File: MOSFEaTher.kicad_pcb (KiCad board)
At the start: 2 copper layers, 63.5 x 51.5 mm, 33 parts, among them J1 GPIO 13, J2 GPIO 12, J3 GPIO 27, J4 GPIO 21, J5 GPIO 33, J6 GPIO 15, J7 GPIO 32, J8 GPIO 14, Q1 STD7NK40Z, Q2 STD7NK40Z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

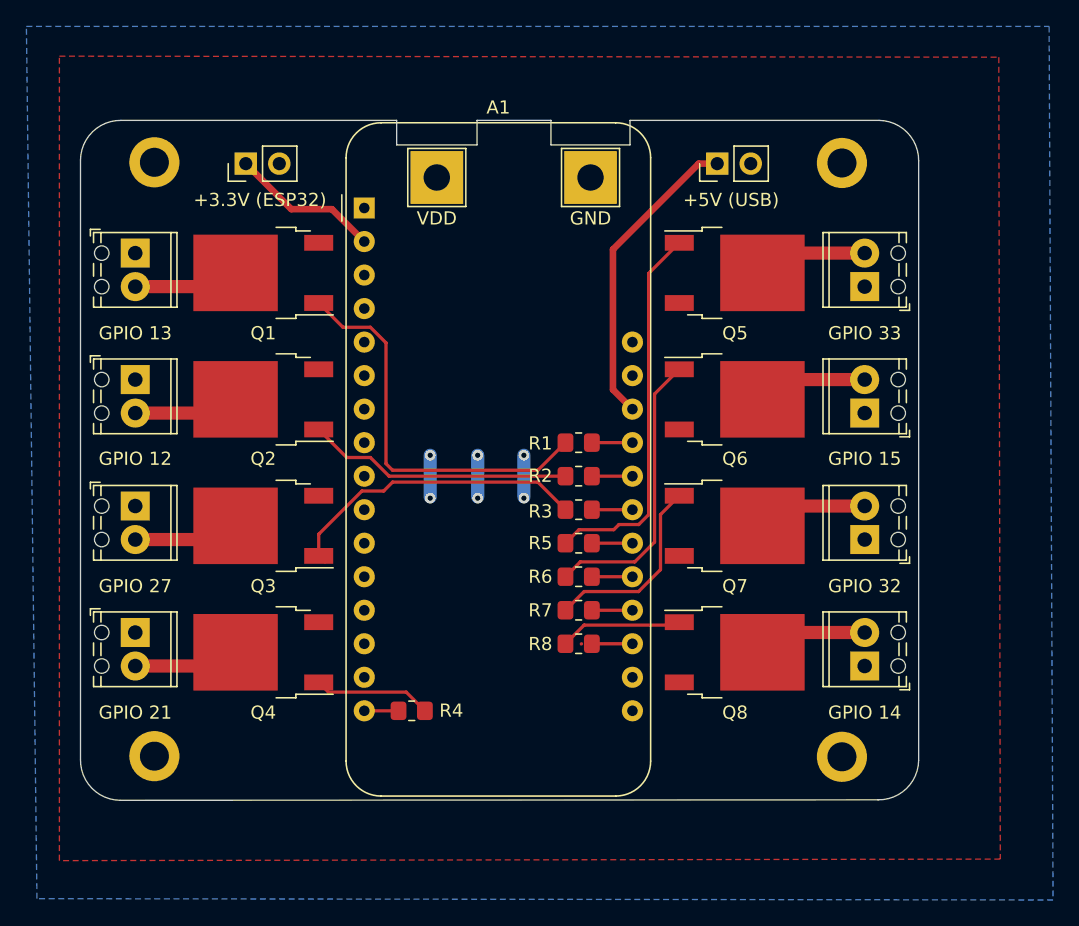
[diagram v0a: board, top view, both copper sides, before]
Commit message: feat: M3 mounting holes, OSHW logo and THM affiliation
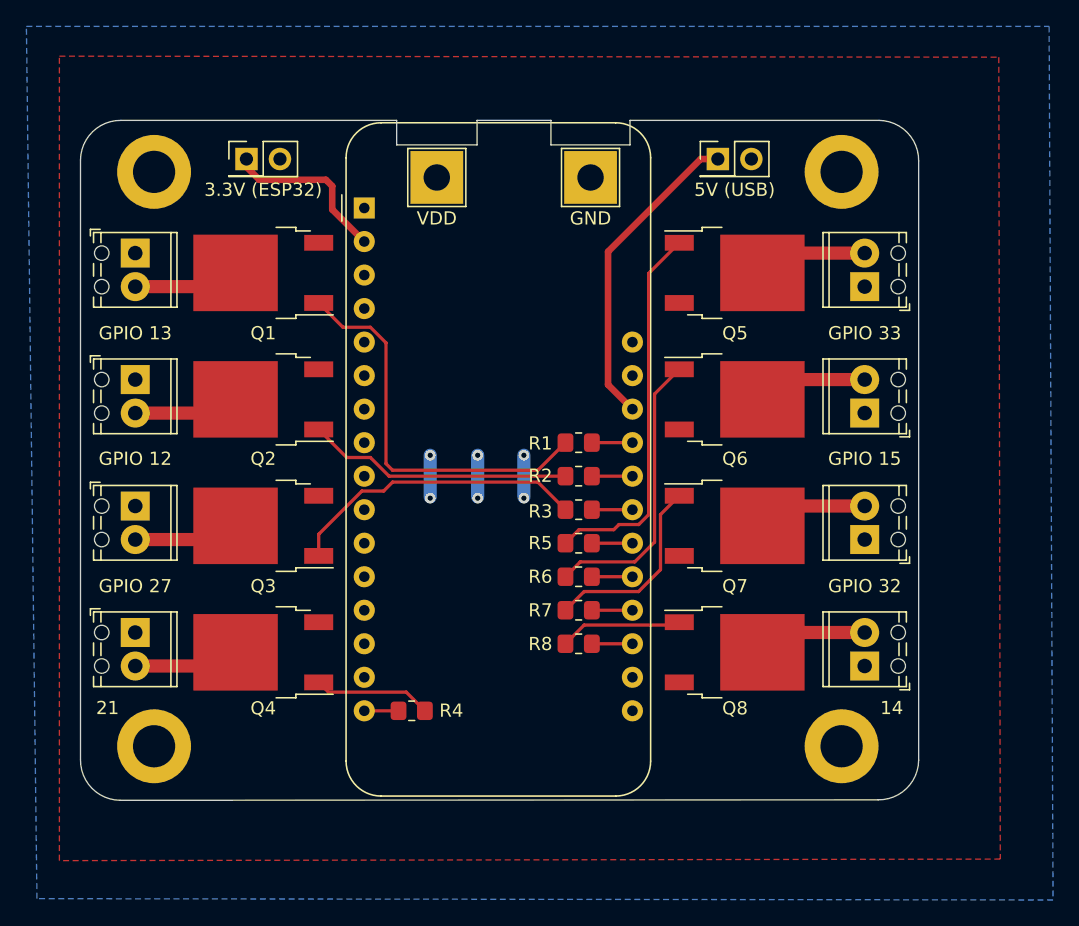
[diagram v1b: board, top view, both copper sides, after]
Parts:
- added REF**: OSHW-Logo2_7.3x6mm_SilkScreen, Symbol:OSHW-Logo2_7.3x6mm_SilkScreen, B.Cu at (68.5, 57.1)
- H1, H2, H3, H4: footprint MountingHole:MountingHole_2.2mm_M2_DIN965_Pad -> MountingHole:MountingHole_3.2mm_M3_DIN965_Pad
- J4: value GPIO 21 -> 21
- J8: value GPIO 14 -> 14
- JP1: value +3.3V (ESP32) -> 3.3V (ESP32); footprint Connector_PinHeader_2.54mm:PinHeader_1x02_P2.54mm_Vertical -> Connector_PinHeader_2.54mm:PinHeader_2x01_P2.54mm_Vertical
- JP2: value +5V (USB) -> 5V (USB); footprint Connector_PinHeader_2.54mm:PinHeader_1x02_P2.54mm_Vertical -> Connector_PinHeader_2.54mm:PinHeader_2x01_P2.54mm_Vertical
- moved H1 0.80 mm to (96.8, 67.0)
- moved H2 0.75 mm to (44.7, 67.0)
- moved H4 0.73 mm to (44.7, 23.5)
- moved H3 0.68 mm to (96.8, 23.5)
- moved JP2 0.35 mm to (87.4, 22.6), turned to 0 degrees
- moved JP1 0.35 mm to (51.7, 22.6), turned to 0 degrees
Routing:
- net +3V3: track 11.4 -> 13.0 mm
- net Net-(Q3-Pad1): track 23.5 -> 22.8 mm
- net +5V: track 23.3 -> 23.9 mm
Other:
- board text added: "MOSFET board for the Adafruit HUZZAH32"
- board text added: "Technische Hochschule Mittelhessen (FB MNI) Author: Martin Weigel License: CC BY 4.0"
- board text added: "V 02"
- board text removed: "MOSFET shield for the Adafruit HUZZAH32"
- board text removed: "Version: 01 Author: Martin Weigel License: CC BY 4.0"

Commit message: feat: better power and signal routing
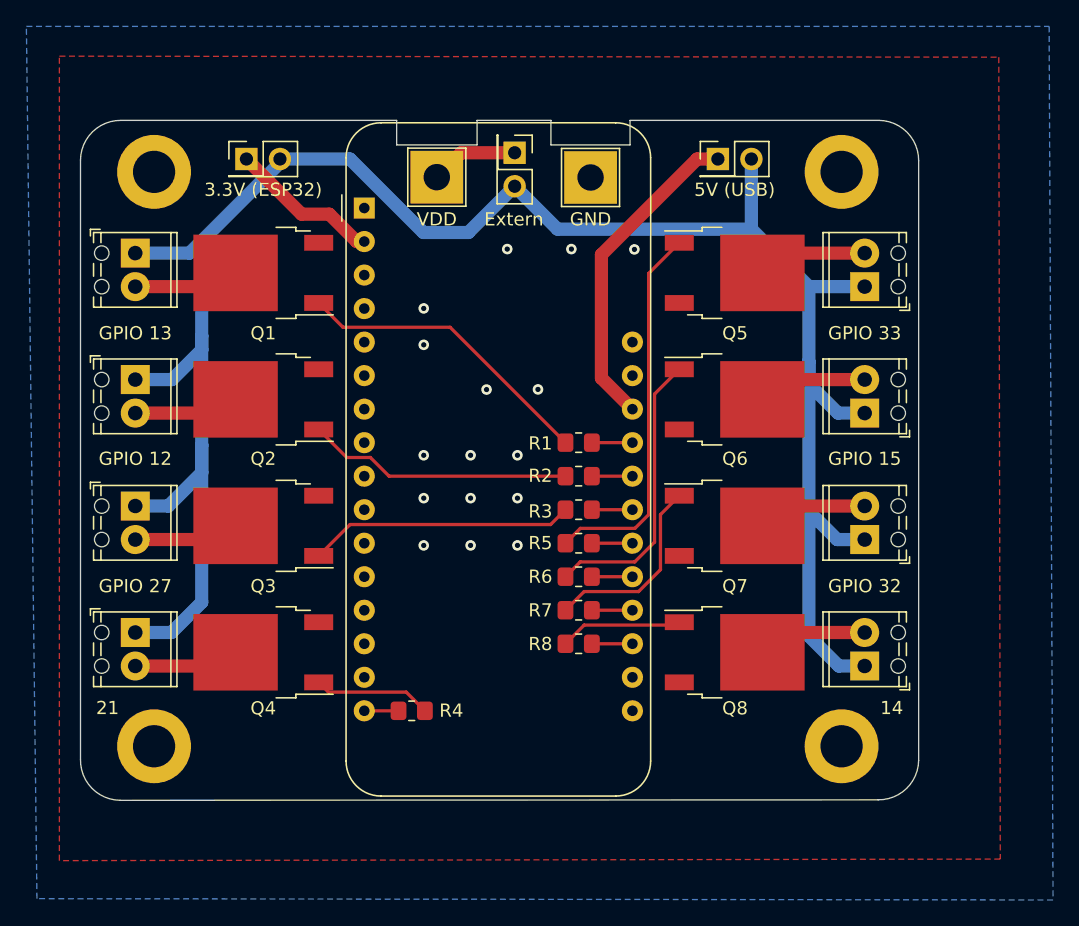
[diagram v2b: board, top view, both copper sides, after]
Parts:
- added JP3: Extern, Connector_PinHeader_2.54mm:PinHeader_2x01_P2.54mm_Vertical, F.Cu at (72.0, 22.1)
- moved REF** 0.91 mm to (68.5, 58.0)
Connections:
- H5 pad 1: VDD -> +12V
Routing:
- net VDD: track 0.00 -> 163.4 mm
- net GND: track 9.45 -> 0.00 mm, vias 6 -> 16
- net Net-(Q1-Pad1): track 30.2 -> 23.1 mm
- net +12V: track 0.00 -> 6.67 mm
- net Net-(Q3-Pad1): track 22.8 -> 20.2 mm
- net +3V3: track 13.0 -> 11.5 mm
- net +5V: track 23.9 -> 24.5 mm
- added copper zone on B.Cu, net GND
- removed copper zone on B.Cu, net VDD
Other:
- board text added: "V 03"
- board text removed: "V 02"
